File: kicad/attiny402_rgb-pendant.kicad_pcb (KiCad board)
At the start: 2 copper layers, 32.8 x 47 mm, 9 parts, among them J1 Conn_01x03_Male, J2 Conn_01x01_Male, J3 Conn_01x01_Male, U1 ATtiny402-SS

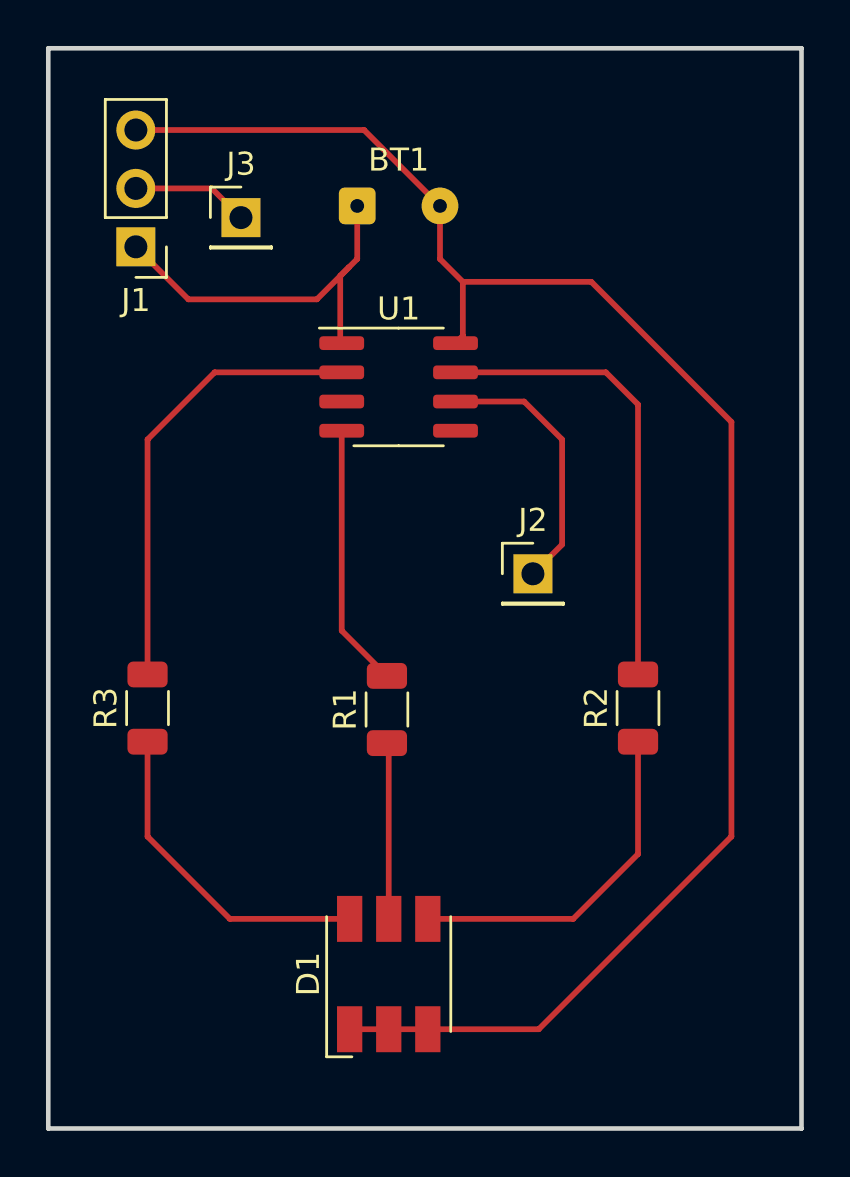
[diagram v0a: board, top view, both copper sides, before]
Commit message: Removed extra programming connector
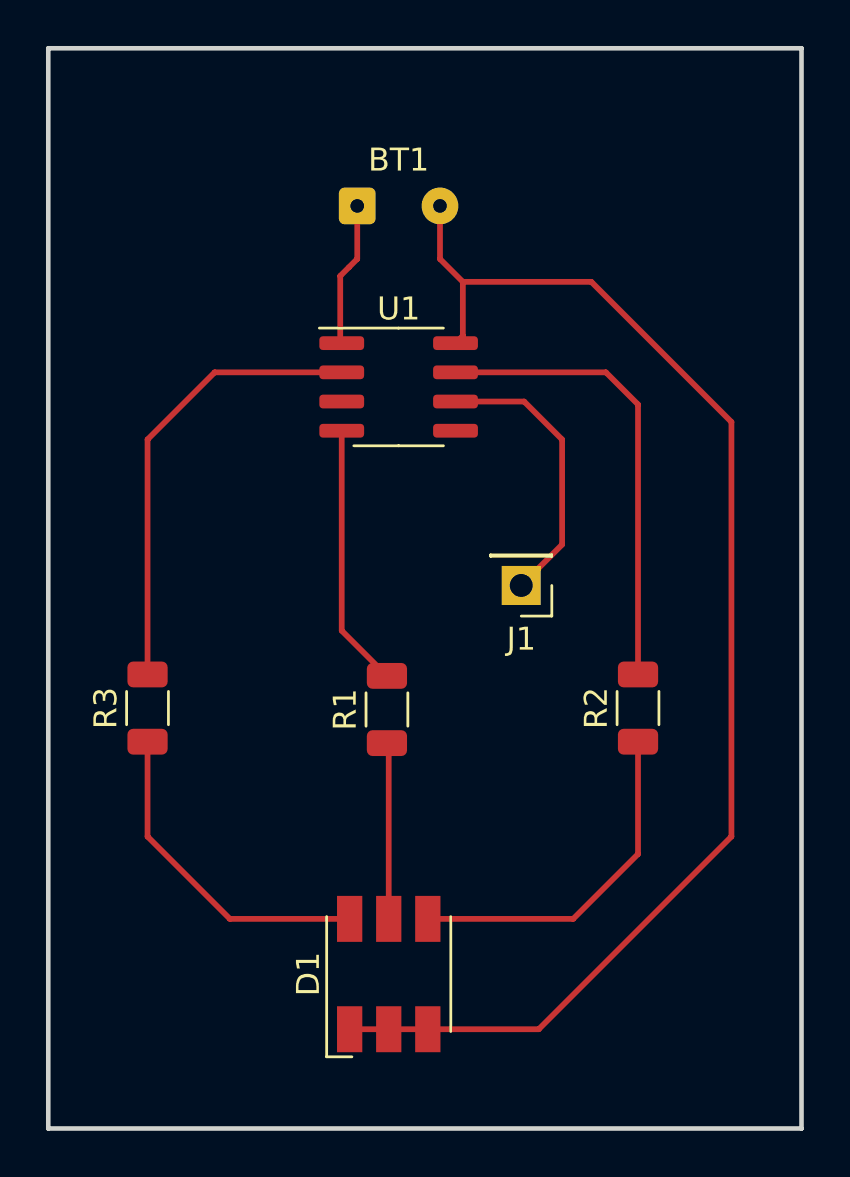
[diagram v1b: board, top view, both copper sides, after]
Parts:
- removed J2, J3: Conn_01x01_Male, Connector_PinHeader_2.54mm:PinHeader_1x01_P2.54mm_Vertical
- J1: value Conn_01x03_Male -> UPDI; footprint Connector_PinHeader_2.54mm:PinHeader_1x03_P2.54mm_Vertical -> Connector_PinHeader_2.54mm:PinHeader_1x01_P2.54mm_Vertical
- moved J1 22.3 mm to (157.5, 88.9)
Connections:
- J1 pad 1: +3V0 -> /UPDI
- U1 pad 4: /RED -> /GREEN
- U1 pad 7: /GREEN -> /RED
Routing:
- net GND: track 73.4 -> 58.8 mm
- net +3V0: track 17.1 -> 6.30 mm
- net Net-(J1-Pad2): track 5.10 -> 0.00 mm
